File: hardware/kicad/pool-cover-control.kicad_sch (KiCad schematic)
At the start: 57 parts, among them J1 Power_Supply _Conn, J3 Key_Switch_Conn, J4 Limit_Switch_Conn, Q1 DMP4015SK3Q-13, U1 STM32G031K8Tx, U2 ULN2003A, U3 LMR14206, U4 PC817, U5 PC817, U6 PC817, U7 PC817

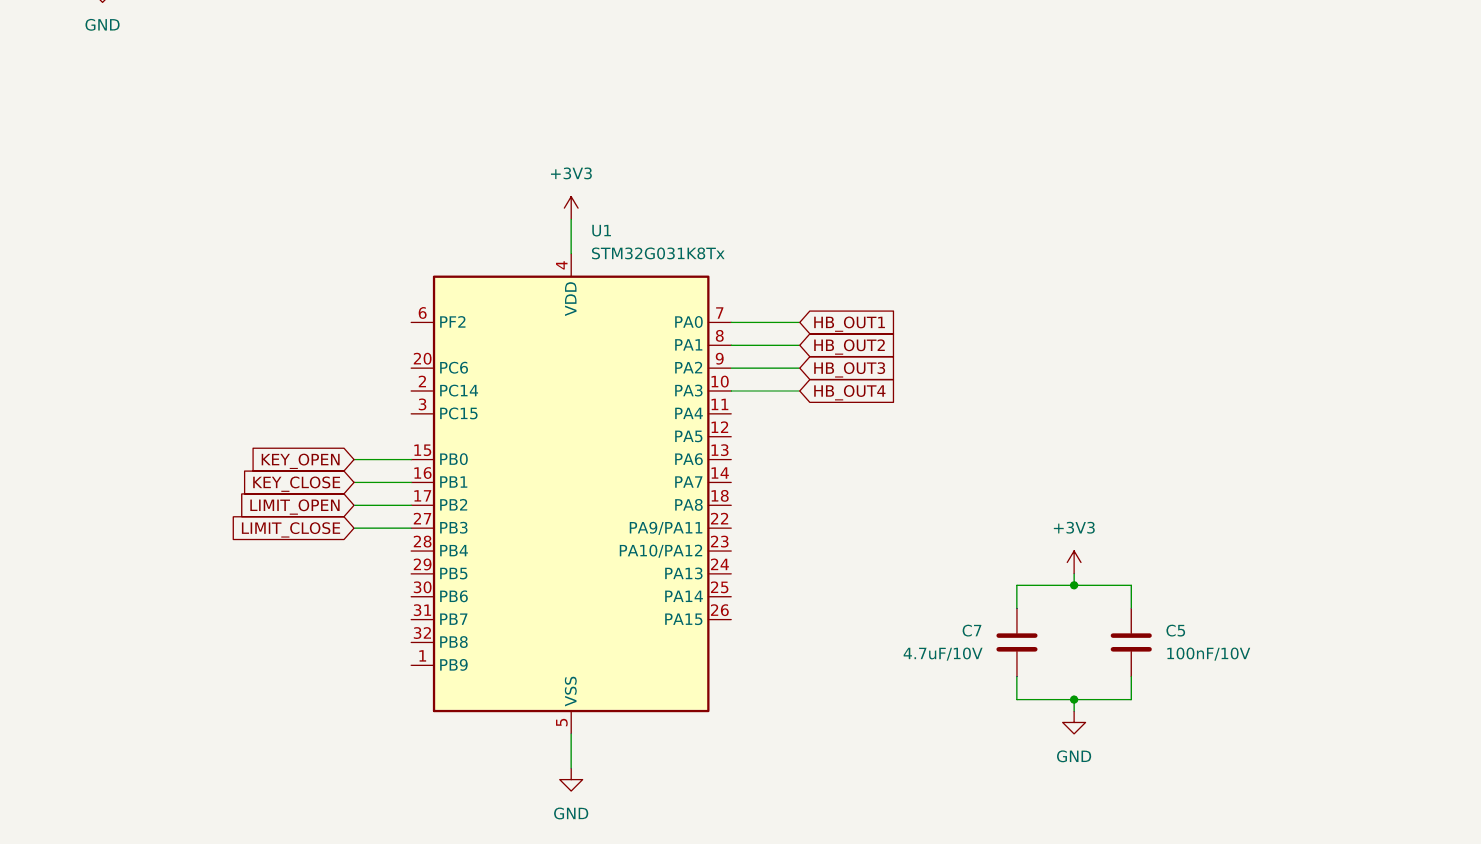
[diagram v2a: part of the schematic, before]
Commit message: feat(hardware): implement SC5 mcu stm32g031 schematic
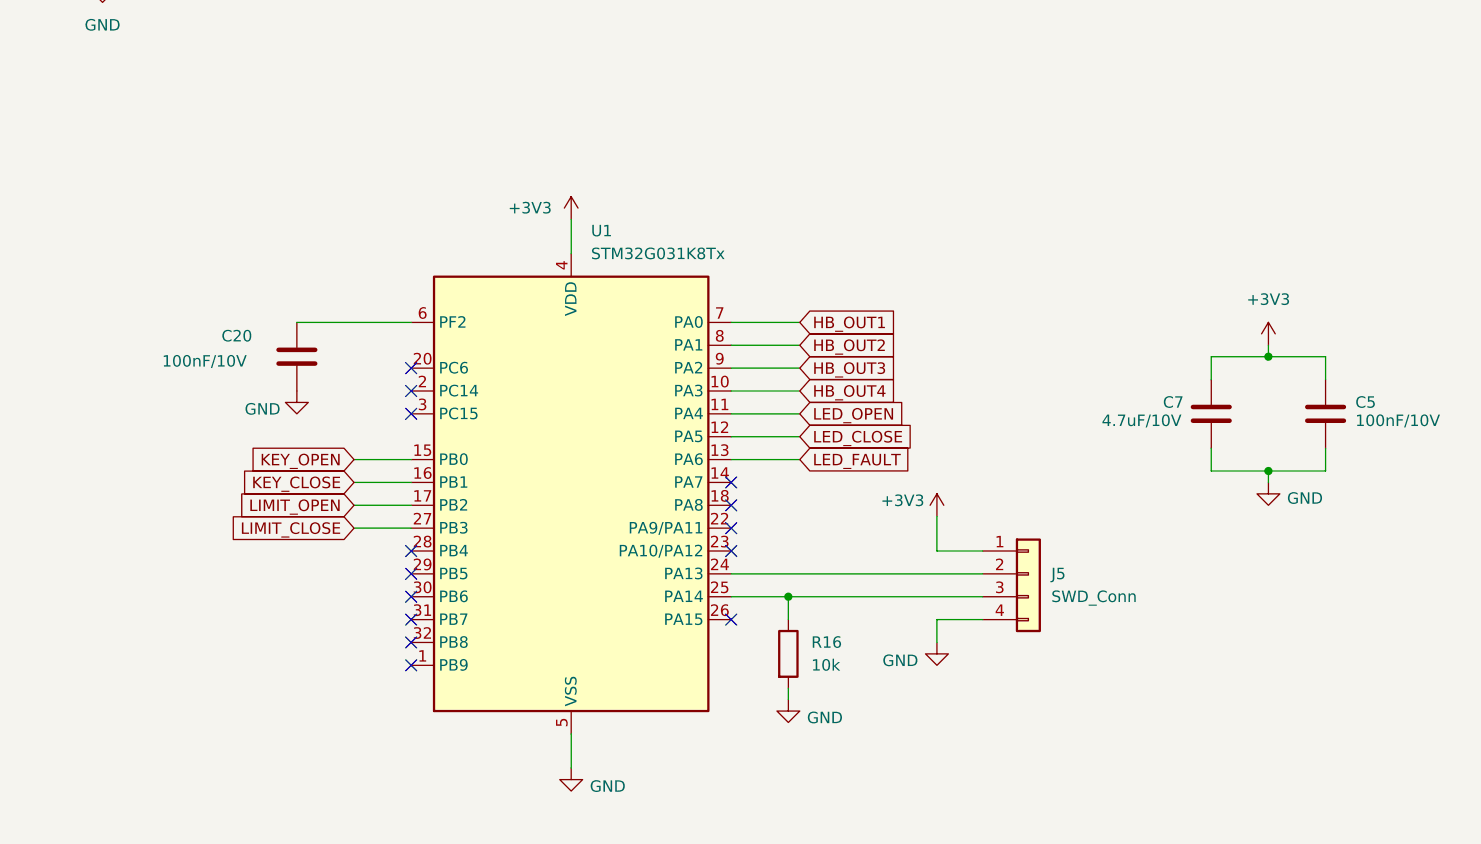
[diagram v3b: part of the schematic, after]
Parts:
- added C20: 100nF/10V, Capacitor_SMD:C_0402_1005Metric, symbol Device:C
- added J5: SWD_Conn, TerminalBlock_Phoenix:TerminalBlock_Phoenix_MKDS-1,5-4-5.08_1x04_P5.08mm_Horizontal, symbol Connector_Generic:Conn_01x04
- added R16: 10k, Resistor_SMD:R_0402_1005Metric, symbol Device:R
- C5: footprint Capacitor_SMD:C_0805_2012Metric -> Capacitor_SMD:C_0402_1005Metric; LCSC (none) -> C162178
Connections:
- net +3V3: now also J5.1 (Pin_1)
- net GND: now also C20.1, J5.4 (Pin_4), R16.2
- net LED_OPEN: now reaches U1.11 (PA4)
- net LED_CLOSE: now reaches U1.12 (PA5)
- net LED_FAULT: now reaches U1.13 (PA6)
- net at U1.24 (PA13): now also J5.2 (Pin_2)
- net at U1.25 (PA14): now also J5.3 (Pin_3), R16.1
- net at U1.6 (PF2): now also C20.2
- no-connect marks 8 -> 22
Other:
- moved on the sheet: C7

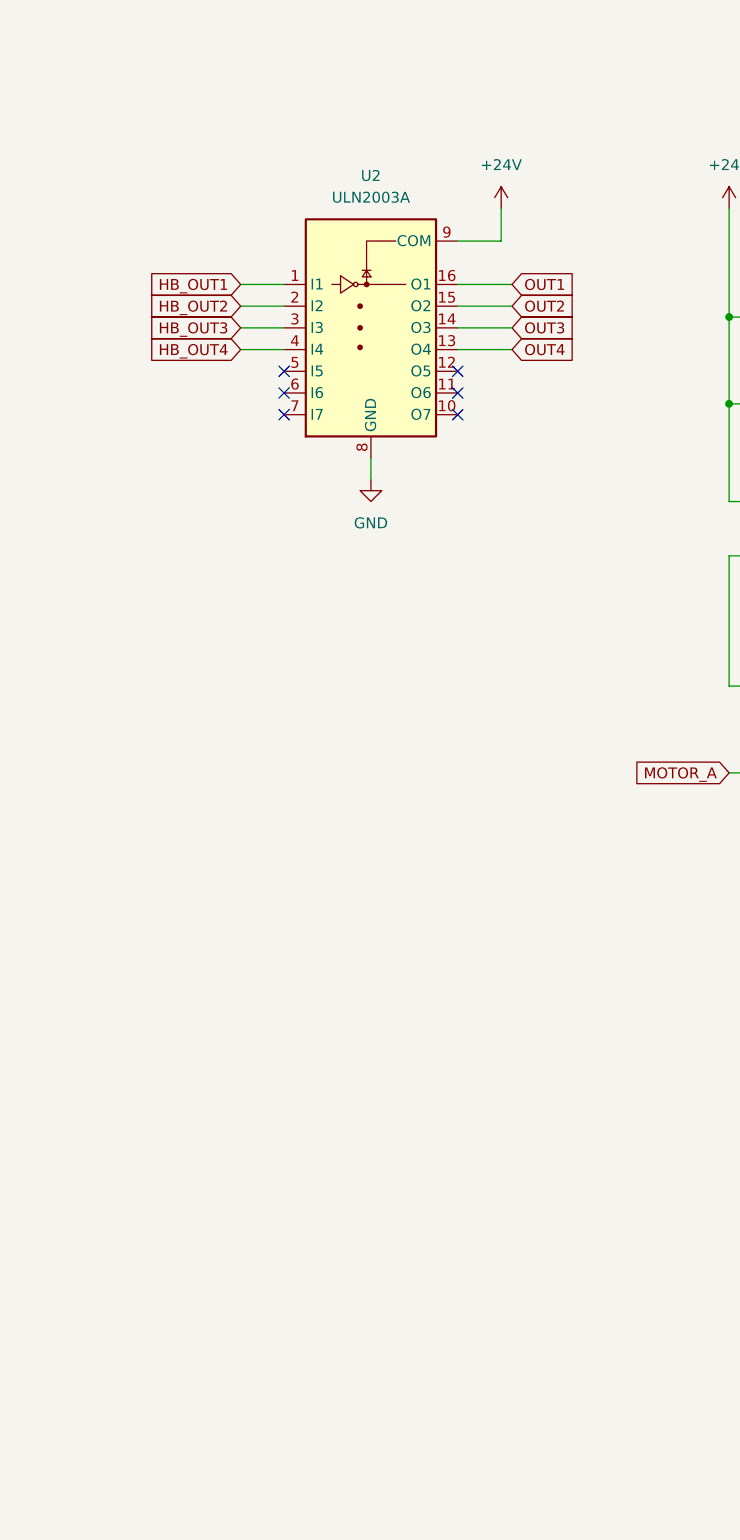
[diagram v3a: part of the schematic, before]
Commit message: feat(hardware): implement SC6 LEDs and SC7 power connectors schematic
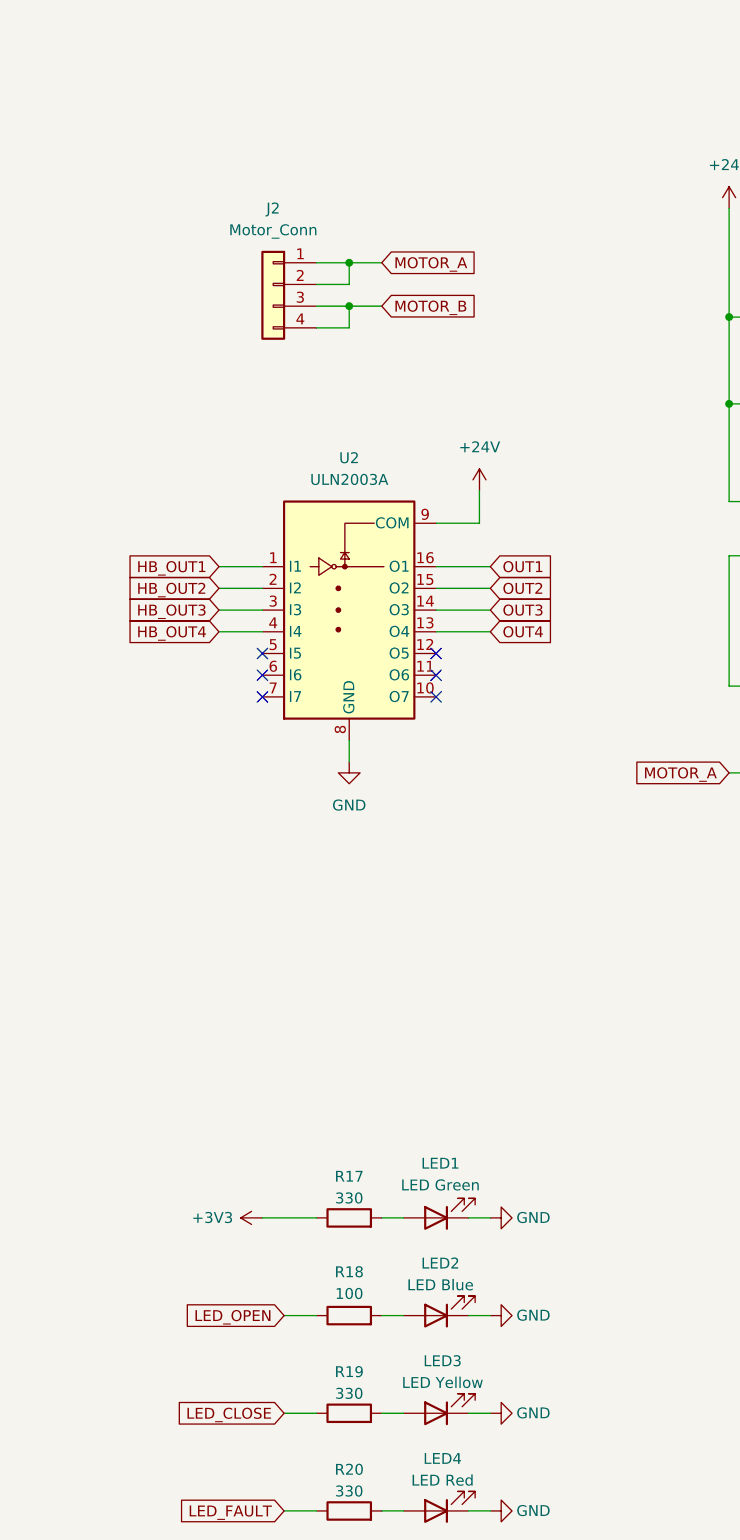
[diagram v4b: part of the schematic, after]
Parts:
- added J2: Motor_Conn, TerminalBlock_Phoenix:TerminalBlock_Phoenix_MKDS-1,5-4-5.08_1x04_P5.08mm_Horizontal, symbol Connector_Generic:Conn_01x04
- added LED1: LED Green, LED_SMD:LED_0603_1608Metric, symbol Device:LED
- added LED2: LED Blue, LED_SMD:LED_0603_1608Metric, symbol Device:LED
- added LED3: LED Yellow, LED_SMD:LED_0603_1608Metric, symbol Device:LED
- added LED4: LED Red, LED_SMD:LED_0603_1608Metric, symbol Device:LED
- added R17, R19, R20: 330, Resistor_SMD:R_0402_1005Metric, symbol Device:R
- added R18: 100, Resistor_SMD:R_0402_1005Metric, symbol Device:R
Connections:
- net +3V3: now also R17.1
- net GND: now also LED1.1 (K), LED2.1 (K), LED3.1 (K), LED4.1 (K)
- net LED_CLOSE: now also R19.1
- net LED_FAULT: now also R20.1
- net LED_OPEN: now also R18.1
- net MOTOR_A: now also J2.1 (Pin_1), J2.2 (Pin_2)
- net MOTOR_B: now also J2.3 (Pin_3), J2.4 (Pin_4)
- new net: LED3.2 (A), R19.2
- new net: LED2.2 (A), R18.2
- new net: LED1.2 (A), R17.2
- new net: LED4.2 (A), R20.2
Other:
- moved on the sheet: U2

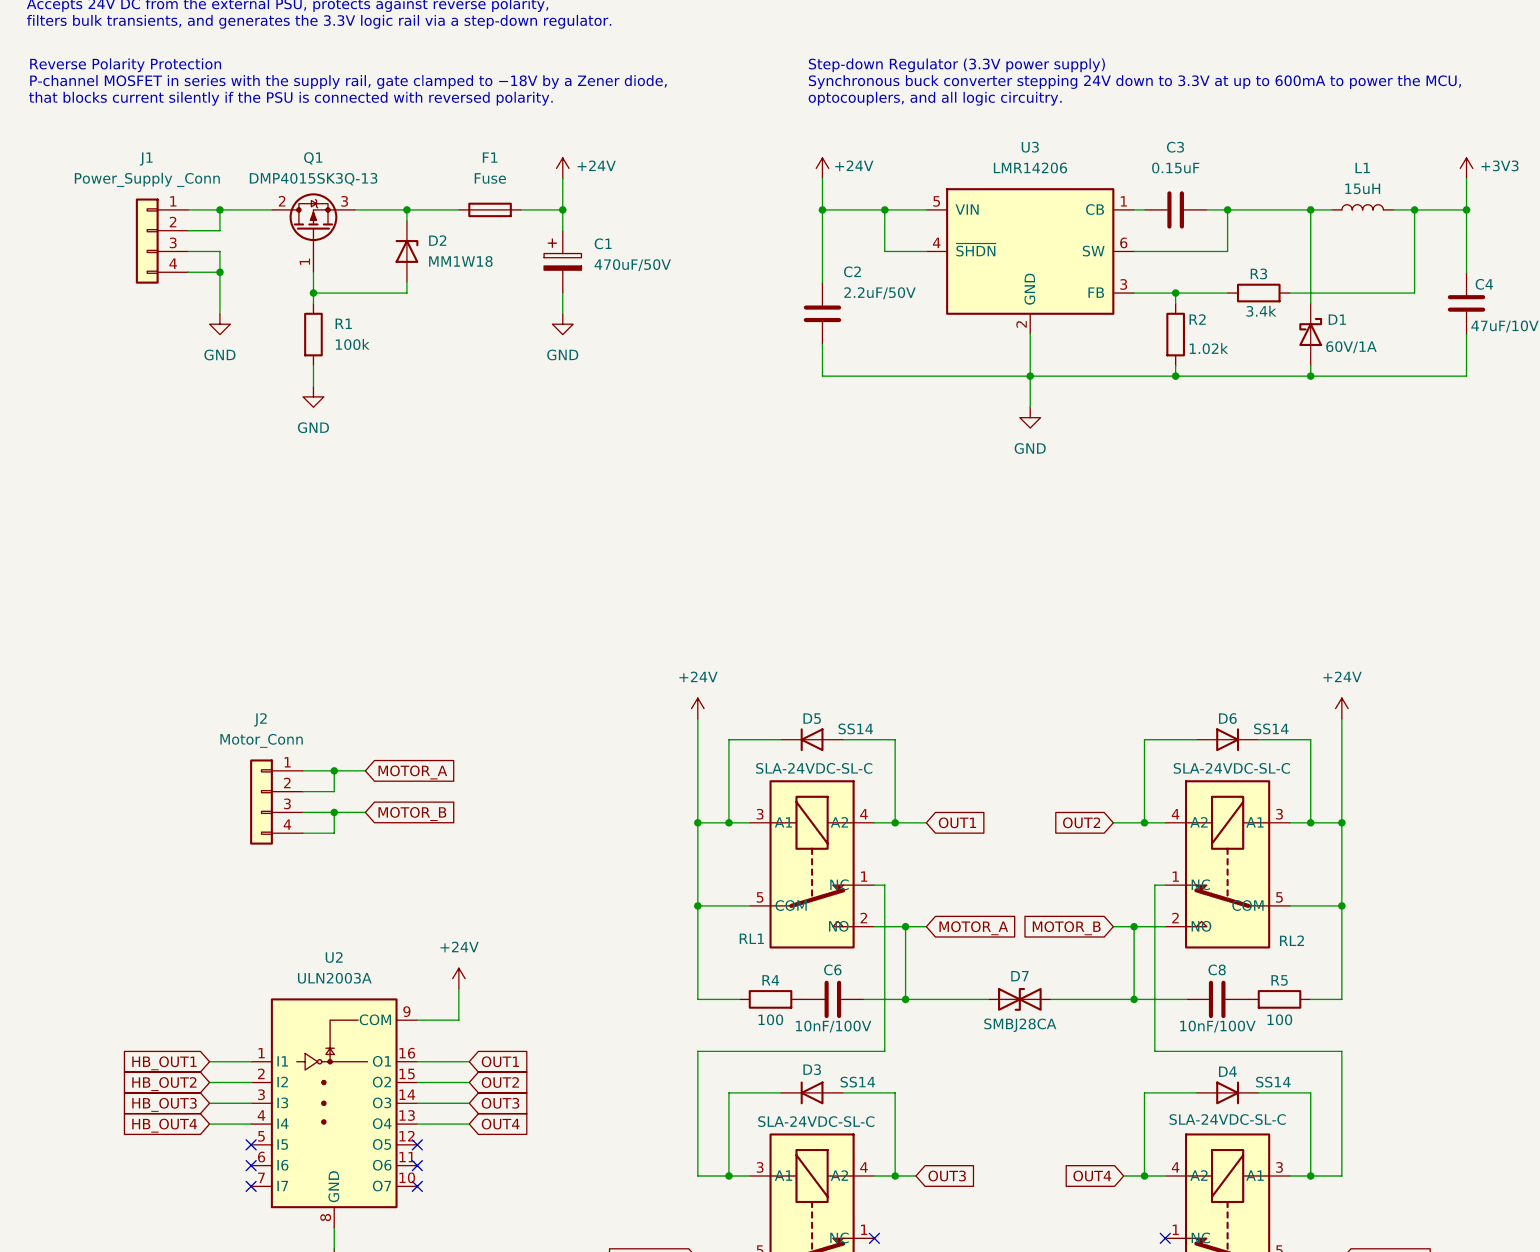
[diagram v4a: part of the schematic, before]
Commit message: feat(hardware): review complete schematic
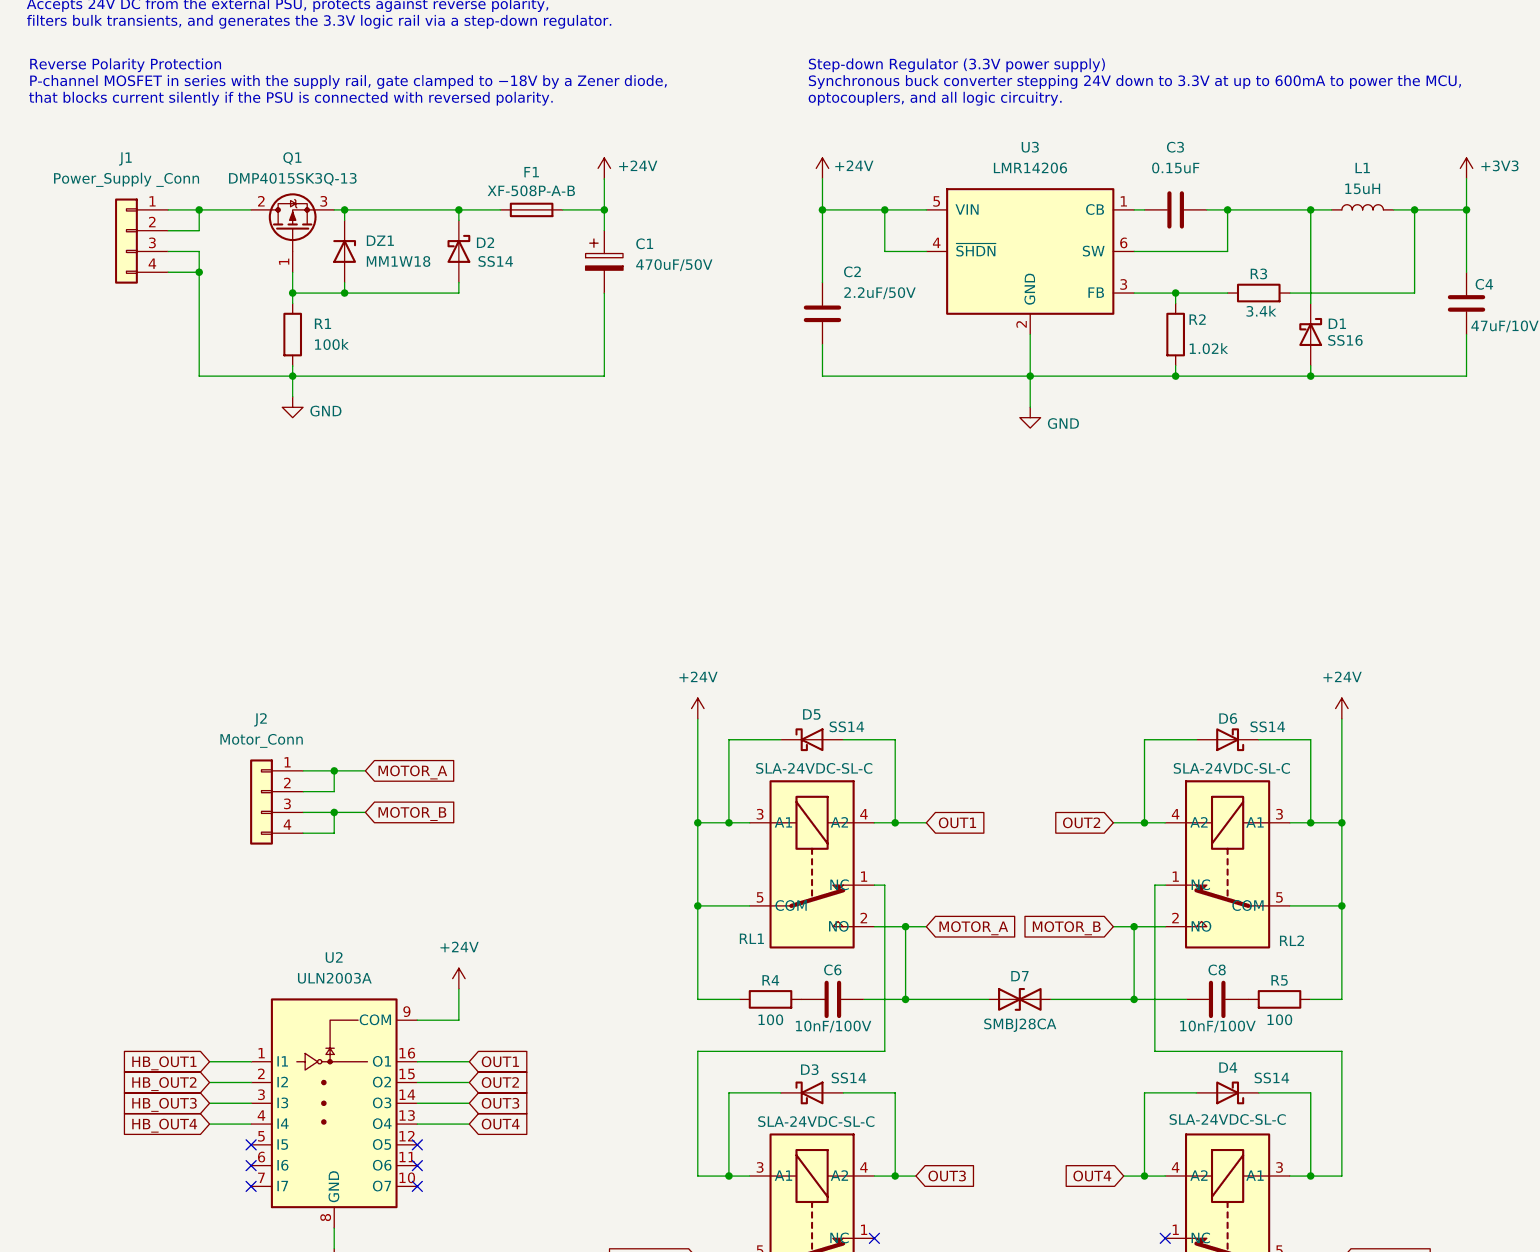
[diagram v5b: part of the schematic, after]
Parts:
- removed D3, D4, D5, D6: SS14, Diode_SMD:D_SMA, symbol Device:D
- added D2, D3, D4, D5, D6: SS14, Diode_SMD:D_SMA, symbol Device:D_Schottky
- C1: LCSC (none) -> C233099
- C2: LCSC (none) -> C2762602
- C3: LCSC (none) -> C513735
- C4: LCSC (none) -> C19103846
- C7: LCSC (none) -> C7472970
- D1: value 60V/1A -> SS16; LCSC (none) -> C908233
- DZ1: renamed from D2; LCSC (none) -> C382948
- F1: value Fuse -> XF-508P-A-B; LCSC (none) -> C19727304
- J3, J4: LCSC (none) -> C91154
- J5: footprint TerminalBlock_Phoenix:TerminalBlock_Phoenix_MKDS-1,5-4-5.08_1x04_P5.08mm_Horizontal -> Connector_PinHeader_2.54mm:PinHeader_1x04_P2.54mm_Vertical; LCSC C90087 -> C2691448
- L1: LCSC (none) -> C1847948
- Q1: LCSC (none) -> C461089
- R1: LCSC (none) -> C2906859
- R12, R13, R8, R9: LCSC C2906864 -> C54532891
- R2: LCSC (none) -> C852594
- R3: LCSC (none) -> C852765
- RL1, RL2, RL3, RL4: footprint pool-cover-control:SLA-24VDC-SL-C -> pool-cover-control:SLA-XXVDC-SL-C
- U1: LCSC (none) -> C724059
- U2: LCSC (none) -> C253892
- U3: LCSC (none) -> C2071127
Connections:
- net +24V: now also D5.1 (K), D6.1 (K)
- net OUT1: now also D5.2 (A)
- net OUT2: now also D6.2 (A)
- net OUT3: now also D3.2 (A)
- net OUT4: now also D4.2 (A)
- net at RL2.1 (NC), RL4.3 (A1): now also D4.1 (K)
- net at RL1.1 (NC), RL3.3 (A1): now also D3.1 (K)
- net at DZ1.1 (K), F1.1, Q1.3 (S): now also D2.1 (K)
- net at DZ1.2 (A), Q1.1 (G), R1.1: now also D2.2 (A)
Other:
- moved on the sheet: C1, DZ1, F1, J1, Q1, R1

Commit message: feat(hardware): implement pcb layout
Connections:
- net PWR_FUSE_IN: now reaches D2.1 (K), DZ1.1 (K), F1.1, Q1.3 (S)
- net PWR_PSU_IN: now reaches J1.1 (Pin_1), J1.2 (Pin_2), Q1.2 (D)
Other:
- moved on the sheet: C1, D2, DZ1, F1, J1, Q1, R1
